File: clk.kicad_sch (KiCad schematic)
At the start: 7 parts, among them U1 4060, U2 4013, Y1 32.768 kHz

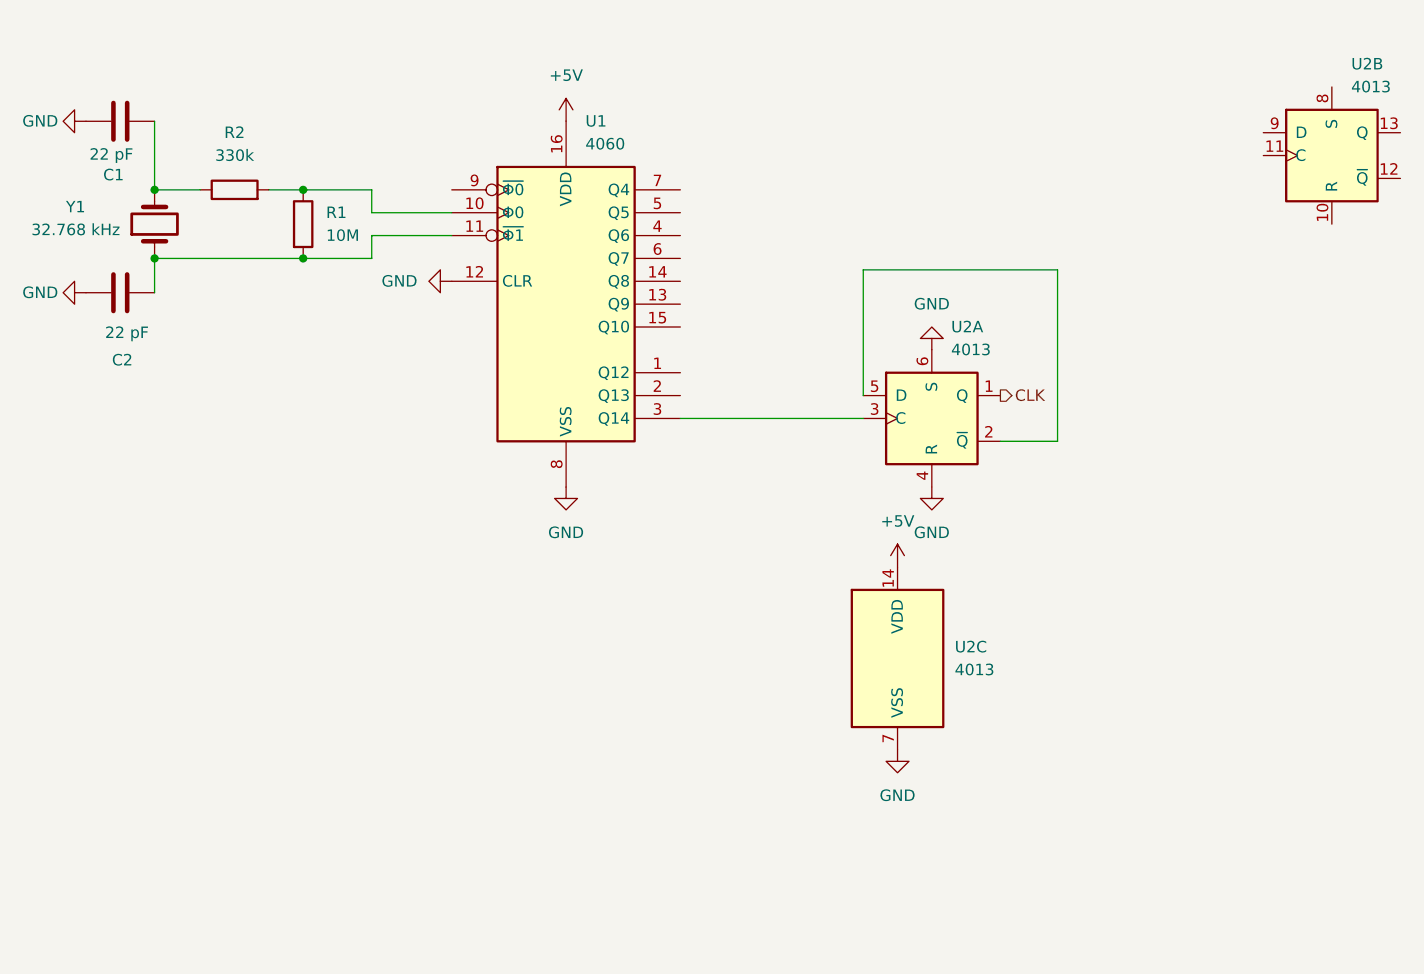
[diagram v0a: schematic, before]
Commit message: CLK circuit finishing the clk circuit
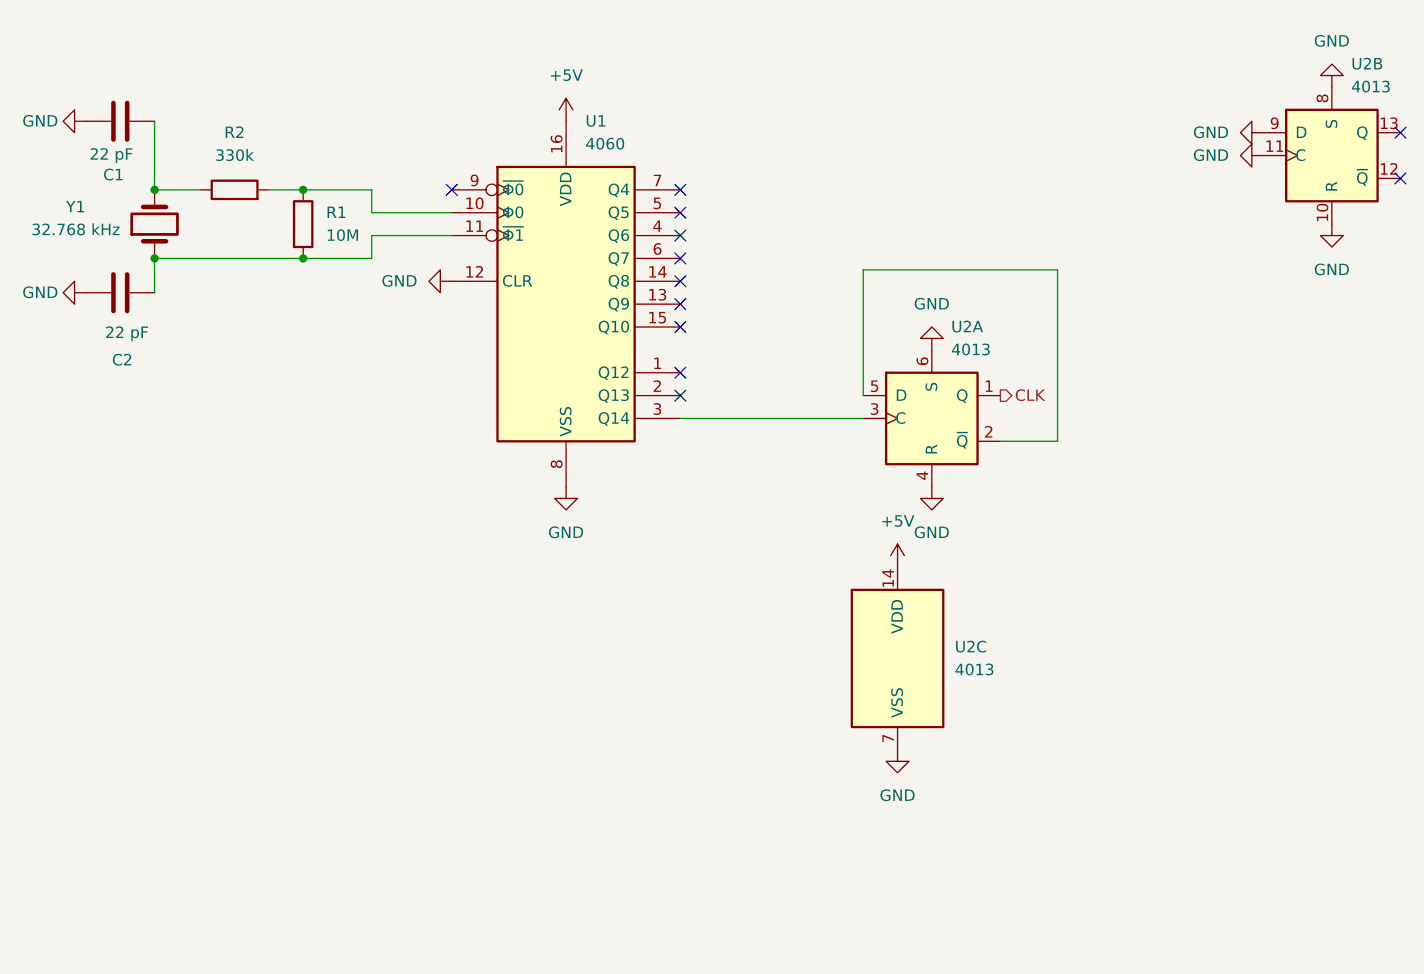
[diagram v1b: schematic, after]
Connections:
- net GND: now also U2.10 (R), U2.11 (C), U2.8 (S), U2.9 (D)
- no-connect marks 0 -> 12

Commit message: Making the circuit for the hour counter
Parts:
- renumbered R2 to R1, R1 to R2
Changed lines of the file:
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@@
 		(in_pos_files yes)
 		(dnp no)
-		(property "Reference" "#PWR05"
+		(property "Reference" "#PWR02"
 			(at 55.88 82.55 0)
 			(hide yes)
@@
 			(project "BinaryClock"
 				(path "/b8db7867-2c41-4996-89b7-85623a375f4b/06cc8139-062b-489e-8e2f-c0ae5744b4b6"
-					(reference "#PWR05")
+					(reference "#PWR02")
 					(unit 1)
 				)
@@
 		(in_pos_files yes)
 		(dnp no)
-		(property "Reference" "#PWR04"
+		(property "Reference" "#PWR01"
 			(at 55.88 63.5 0)
 			(hide yes)
@@
 			(project "BinaryClock"
 				(path "/b8db7867-2c41-4996-89b7-85623a375f4b/06cc8139-062b-489e-8e2f-c0ae5744b4b6"
-					(reference "#PWR04")
+					(reference "#PWR01")
 					(unit 1)
 				)
@@
 		(dnp no)
 		(fields_autoplaced yes)
-		(property "Reference" "#PWR08"
+		(property "Reference" "#PWR06"
 			(at 152.4 116.84 0)
 			(hide yes)
@@
 			(project "BinaryClock"
 				(path "/b8db7867-2c41-4996-89b7-85623a375f4b/06cc8139-062b-489e-8e2f-c0ae5744b4b6"
-					(reference "#PWR08")
+					(reference "#PWR06")
 					(unit 1)
 				)
@@
 		(dnp no)
 		(fields_autoplaced yes)
-		(property "Reference" "#PWR01"
+		(property "Reference" "#PWR04"
 			(at 115.57 67.31 0)
 			(hide yes)
@@
 			(project "BinaryClock"
 				(path "/b8db7867-2c41-4996-89b7-85623a375f4b/06cc8139-062b-489e-8e2f-c0ae5744b4b6"
-					(reference "#PWR01")
+					(reference "#PWR04")
 					(unit 1)
 				)
@@
 		(dnp no)
 		(fields_autoplaced yes)
-		(property "Reference" "R2"
+		(property "Reference" "R1"
 			(at 78.74 64.77 90)
 			(show_name no)
@@
 			(project "BinaryClock"
 				(path "/b8db7867-2c41-4996-89b7-85623a375f4b/06cc8139-062b-489e-8e2f-c0ae5744b4b6"
-					(reference "R2")
+					(reference "R1")
 					(unit 1)
 				)
@@
 		(dnp no)
 		(fields_autoplaced yes)
-		(property "Reference" "#PWR06"
+		(property "Reference" "#PWR09"
 			(at 156.21 110.49 0)
 			(hide yes)
@@
 			(project "BinaryClock"
 				(path "/b8db7867-2c41-4996-89b7-85623a375f4b/06cc8139-062b-489e-8e2f-c0ae5744b4b6"
-					(reference "#PWR06")
+					(reference "#PWR09")
 					(unit 1)
 				)
@@
 		(dnp no)
 		(fields_autoplaced yes)
-		(property "Reference" "#PWR011"
+		(property "Reference" "#PWR010"
 			(at 186.69 64.77 0)
 			(hide yes)
@@
 			(project "BinaryClock"
 				(path "/b8db7867-2c41-4996-89b7-85623a375f4b/06cc8139-062b-489e-8e2f-c0ae5744b4b6"
-					(reference "#PWR011")
+					(reference "#PWR010")
 					(unit 1)
 				)
@@
 		(dnp no)
 		(fields_autoplaced yes)
-		(property "Reference" "#PWR07"
+		(property "Reference" "#PWR08"
 			(at 156.21 82.55 0)
 			(hide yes)
@@
 			(project "BinaryClock"
 				(path "/b8db7867-2c41-4996-89b7-85623a375f4b/06cc8139-062b-489e-8e2f-c0ae5744b4b6"
-					(reference "#PWR07")
+					(reference "#PWR08")
 					(unit 1)
 				)
@@
 		(dnp no)
 		(fields_autoplaced yes)
-		(property "Reference" "R1"
+		(property "Reference" "R2"
 			(at 88.9 73.6599 0)
 			(show_name no)
@@
 			(project "BinaryClock"
 				(path "/b8db7867-2c41-4996-89b7-85623a375f4b/06cc8139-062b-489e-8e2f-c0ae5744b4b6"
-					(reference "R1")
+					(reference "R2")
 					(unit 1)
 				)
@@
 		(dnp no)
 		(fields_autoplaced yes)
-		(property "Reference" "#PWR09"
+		(property "Reference" "#PWR07"
 			(at 152.4 139.7 0)
 			(hide yes)
@@
 			(project "BinaryClock"
 				(path "/b8db7867-2c41-4996-89b7-85623a375f4b/06cc8139-062b-489e-8e2f-c0ae5744b4b6"
-					(reference "#PWR09")
+					(reference "#PWR07")
 					(unit 1)
 				)
@@
 		(dnp no)
 		(fields_autoplaced yes)
-		(property "Reference" "#PWR010"
+		(property "Reference" "#PWR012"
 			(at 200.66 53.34 0)
 			(hide yes)
@@
 			(project "BinaryClock"
 				(path "/b8db7867-2c41-4996-89b7-85623a375f4b/06cc8139-062b-489e-8e2f-c0ae5744b4b6"
-					(reference "#PWR010")
+					(reference "#PWR012")
 					(unit 1)
 				)
@@
 		(dnp no)
 		(fields_autoplaced yes)
-		(property "Reference" "#PWR012"
+		(property "Reference" "#PWR011"
 			(at 186.69 67.31 0)
 			(hide yes)
@@
 			(project "BinaryClock"
 				(path "/b8db7867-2c41-4996-89b7-85623a375f4b/06cc8139-062b-489e-8e2f-c0ae5744b4b6"
-					(reference "#PWR012")
+					(reference "#PWR011")
 					(unit 1)
 				)
@@
 		(dnp no)
 		(fields_autoplaced yes)
-		(property "Reference" "#PWR02"
+		(property "Reference" "#PWR05"
 			(at 115.57 110.49 0)
 			(hide yes)
@@
 			(project "BinaryClock"
 				(path "/b8db7867-2c41-4996-89b7-85623a375f4b/06cc8139-062b-489e-8e2f-c0ae5744b4b6"
-					(reference "#PWR02")
-					(unit 1)
-				)
+					(reference "#PWR05")
+					(unit 1)
+				)

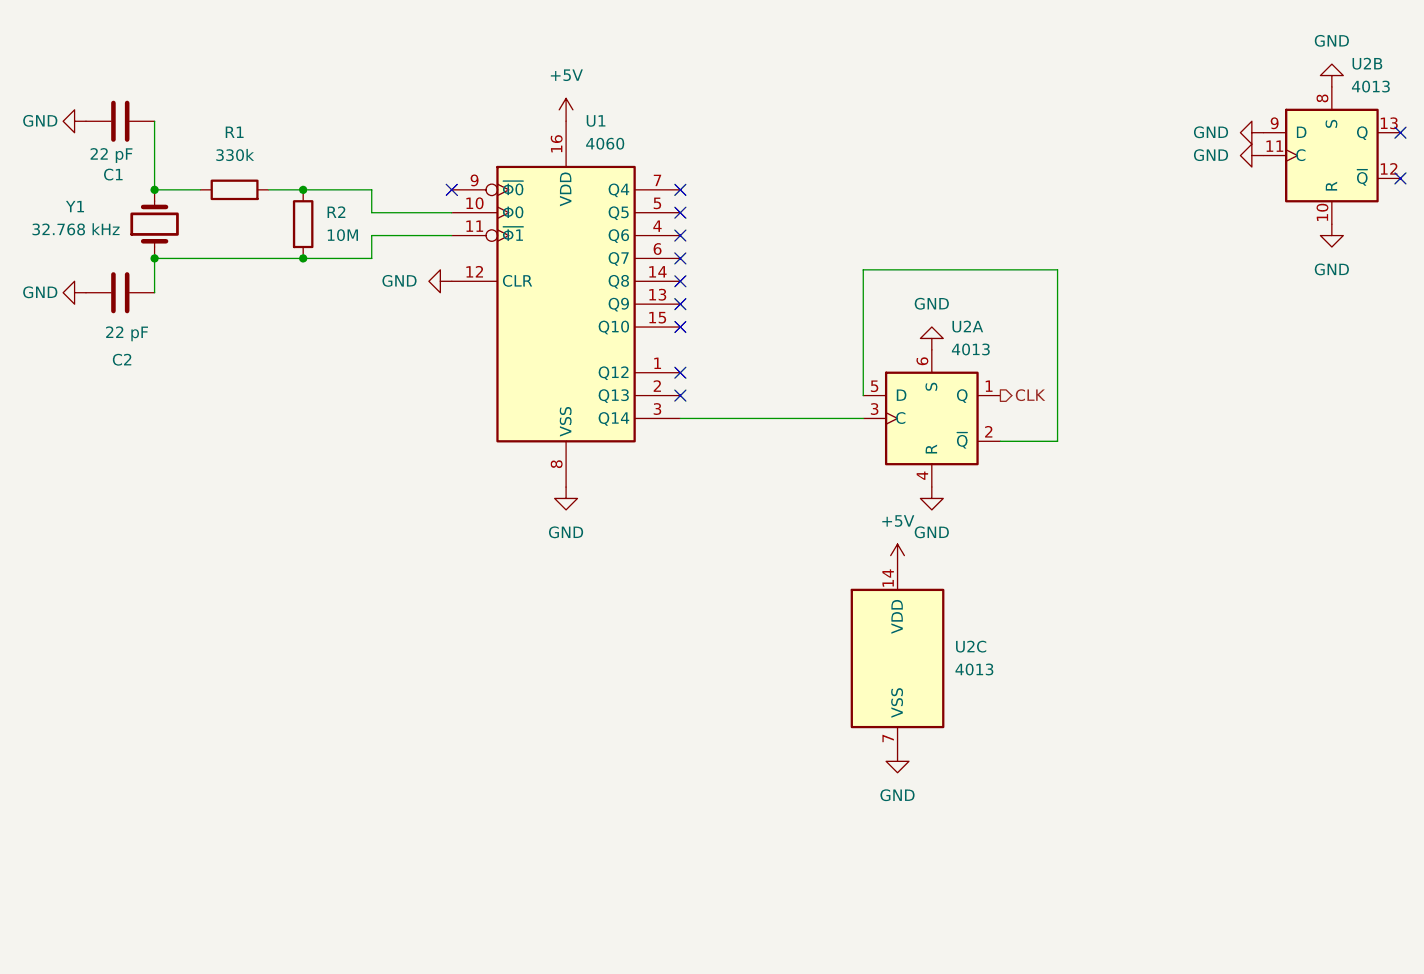
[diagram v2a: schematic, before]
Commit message: Making the 24 rst for ewery counter and adding Capacitors
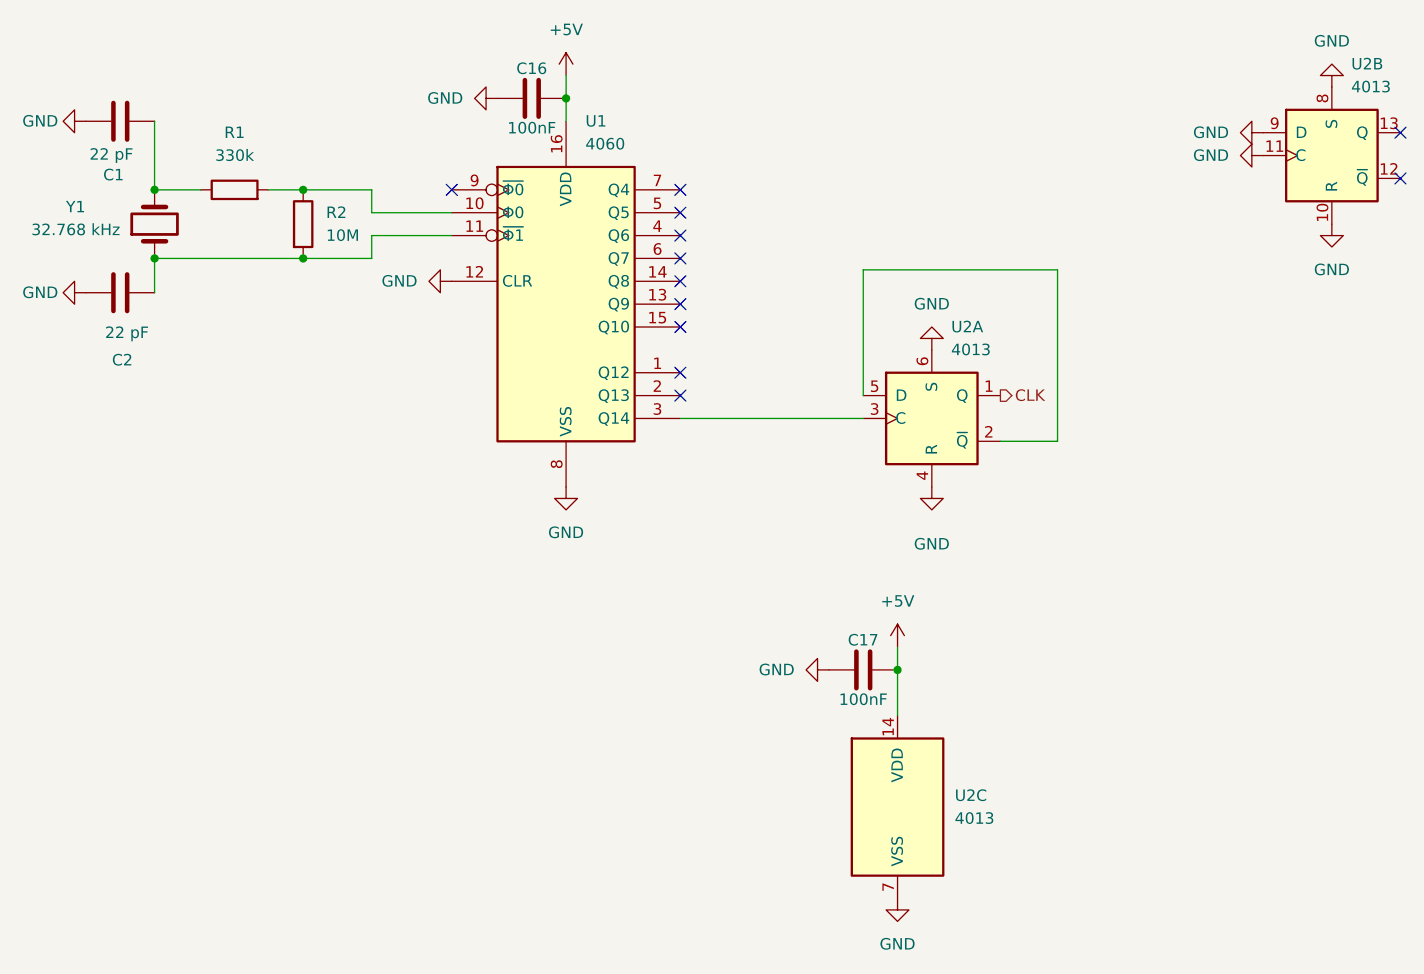
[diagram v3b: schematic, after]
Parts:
- added C16, C17: 100nF, symbol Device:C
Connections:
- net +5V: now also C16.2, C17.2
- net GND: now also C16.1, C17.1
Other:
- moved on the sheet: U2C

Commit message: Cleaning the shematic
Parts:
- renumbered C16 to C3, C17 to C4
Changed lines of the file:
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@@
 		(dnp no)
 		(fields_autoplaced yes)
-		(property "Reference" "#PWR0109"
+		(property "Reference" "#PWR07"
 			(at 138.43 124.46 0)
 			(hide yes)
@@
 			(project "BinaryClock"
 				(path "/b8db7867-2c41-4996-89b7-85623a375f4b/06cc8139-062b-489e-8e2f-c0ae5744b4b6"
-					(reference "#PWR0109")
+					(reference "#PWR07")
 					(unit 1)
 				)
@@
 		(dnp no)
 		(fields_autoplaced yes)
-		(property "Reference" "#PWR0107"
+		(property "Reference" "#PWR04"
 			(at 101.6 60.96 0)
 			(hide yes)
@@
 			(project "BinaryClock"
 				(path "/b8db7867-2c41-4996-89b7-85623a375f4b/06cc8139-062b-489e-8e2f-c0ae5744b4b6"
-					(reference "#PWR0107")
+					(reference "#PWR04")
 					(unit 1)
 				)
@@
 		(dnp no)
 		(fields_autoplaced yes)
-		(property "Reference" "#PWR013"
+		(property "Reference" "#PWR015"
 			(at 200.66 81.28 0)
 			(hide yes)
@@
 			(project "BinaryClock"
 				(path "/b8db7867-2c41-4996-89b7-85623a375f4b/06cc8139-062b-489e-8e2f-c0ae5744b4b6"
-					(reference "#PWR013")
+					(reference "#PWR015")
 					(unit 1)
 				)
@@
 		(in_pos_files yes)
 		(dnp no)
-		(property "Reference" "#PWR09"
+		(property "Reference" "#PWR011"
 			(at 156.21 110.49 0)
 			(hide yes)
@@
 			(project "BinaryClock"
 				(path "/b8db7867-2c41-4996-89b7-85623a375f4b/06cc8139-062b-489e-8e2f-c0ae5744b4b6"
-					(reference "#PWR09")
+					(reference "#PWR011")
 					(unit 1)
 				)
@@
 		(dnp no)
 		(fields_autoplaced yes)
-		(property "Reference" "#PWR010"
+		(property "Reference" "#PWR012"
 			(at 186.69 64.77 0)
 			(hide yes)
@@
 			(project "BinaryClock"
 				(path "/b8db7867-2c41-4996-89b7-85623a375f4b/06cc8139-062b-489e-8e2f-c0ae5744b4b6"
-					(reference "#PWR010")
+					(reference "#PWR012")
 					(unit 1)
 				)
@@
 		(dnp no)
 		(fields_autoplaced yes)
-		(property "Reference" "#PWR08"
+		(property "Reference" "#PWR010"
 			(at 156.21 82.55 0)
 			(hide yes)
@@
 			(project "BinaryClock"
 				(path "/b8db7867-2c41-4996-89b7-85623a375f4b/06cc8139-062b-489e-8e2f-c0ae5744b4b6"
-					(reference "#PWR08")
+					(reference "#PWR010")
 					(unit 1)
 				)
@@
 		(dnp no)
 		(fields_autoplaced yes)
-		(property "Reference" "#PWR0110"
+		(property "Reference" "#PWR08"
 			(at 152.4 125.73 0)
 			(hide yes)
@@
 			(project "BinaryClock"
 				(path "/b8db7867-2c41-4996-89b7-85623a375f4b/06cc8139-062b-489e-8e2f-c0ae5744b4b6"
-					(reference "#PWR0110")
+					(reference "#PWR08")
 					(unit 1)
 				)
@@
 		(dnp no)
 		(fields_autoplaced yes)
-		(property "Reference" "#PWR07"
+		(property "Reference" "#PWR09"
 			(at 152.4 156.21 0)
 			(hide yes)
@@
 			(project "BinaryClock"
 				(path "/b8db7867-2c41-4996-89b7-85623a375f4b/06cc8139-062b-489e-8e2f-c0ae5744b4b6"
-					(reference "#PWR07")
+					(reference "#PWR09")
 					(unit 1)
 				)
@@
 		(dnp no)
 		(fields_autoplaced yes)
-		(property "Reference" "#PWR012"
+		(property "Reference" "#PWR014"
 			(at 200.66 53.34 0)
 			(hide yes)
@@
 			(project "BinaryClock"
 				(path "/b8db7867-2c41-4996-89b7-85623a375f4b/06cc8139-062b-489e-8e2f-c0ae5744b4b6"
-					(reference "#PWR012")
+					(reference "#PWR014")
 					(unit 1)
 				)
@@
 		(in_pos_files yes)
 		(dnp no)
-		(property "Reference" "C17"
+		(property "Reference" "C4"
 			(at 148.59 121.158 90)
 			(show_name no)
@@
 			(project "BinaryClock"
 				(path "/b8db7867-2c41-4996-89b7-85623a375f4b/06cc8139-062b-489e-8e2f-c0ae5744b4b6"
-					(reference "C17")
+					(reference "C4")
 					(unit 1)
 				)
@@
 		(dnp no)
 		(fields_autoplaced yes)
-		(property "Reference" "#PWR0108"
+		(property "Reference" "#PWR05"
 			(at 115.57 62.23 0)
 			(hide yes)
@@
 			(project "BinaryClock"
 				(path "/b8db7867-2c41-4996-89b7-85623a375f4b/06cc8139-062b-489e-8e2f-c0ae5744b4b6"
-					(reference "#PWR0108")
+					(reference "#PWR05")
 					(unit 1)
 				)
@@
 		(in_pos_files yes)
 		(dnp no)
-		(property "Reference" "C16"
+		(property "Reference" "C3"
 			(at 111.76 57.658 90)
 			(show_name no)
@@
 			(project "BinaryClock"
 				(path "/b8db7867-2c41-4996-89b7-85623a375f4b/06cc8139-062b-489e-8e2f-c0ae5744b4b6"
-					(reference "C16")
+					(reference "C3")
 					(unit 1)
 				)
@@
 		(dnp no)
 		(fields_autoplaced yes)
-		(property "Reference" "#PWR011"
+		(property "Reference" "#PWR013"
 			(at 186.69 67.31 0)
 			(hide yes)
@@
 			(project "BinaryClock"
 				(path "/b8db7867-2c41-4996-89b7-85623a375f4b/06cc8139-062b-489e-8e2f-c0ae5744b4b6"
-					(reference "#PWR011")
+					(reference "#PWR013")
 					(unit 1)
 				)
@@
 		(dnp no)
 		(fields_autoplaced yes)
-		(property "Reference" "#PWR05"
+		(property "Reference" "#PWR06"
 			(at 115.57 110.49 0)
 			(hide yes)
@@
 			(project "BinaryClock"
 				(path "/b8db7867-2c41-4996-89b7-85623a375f4b/06cc8139-062b-489e-8e2f-c0ae5744b4b6"
-					(reference "#PWR05")
-					(unit 1)
-				)
+					(reference "#PWR06")
+					(unit 1)
+				)
